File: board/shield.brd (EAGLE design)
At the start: 66 x 57.8 mm, 44 parts, among them IC1 LM75, J1 WEALTHMETAL DS-214B, J2 22-05-7028-02, J3 22-05-7038-03, K1 G5L, T1 BC817, U1 LM2596S-5.0

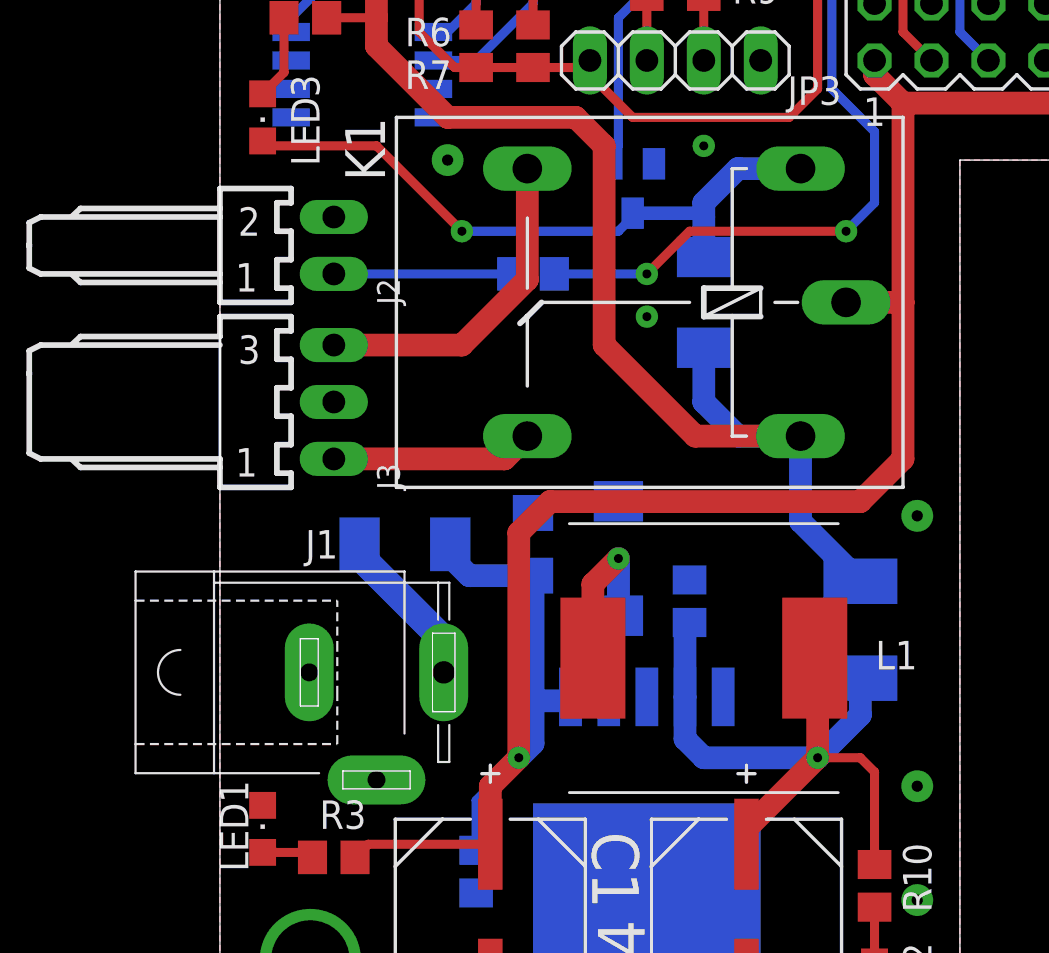
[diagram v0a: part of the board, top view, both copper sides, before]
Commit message: DC Jack connector replaced
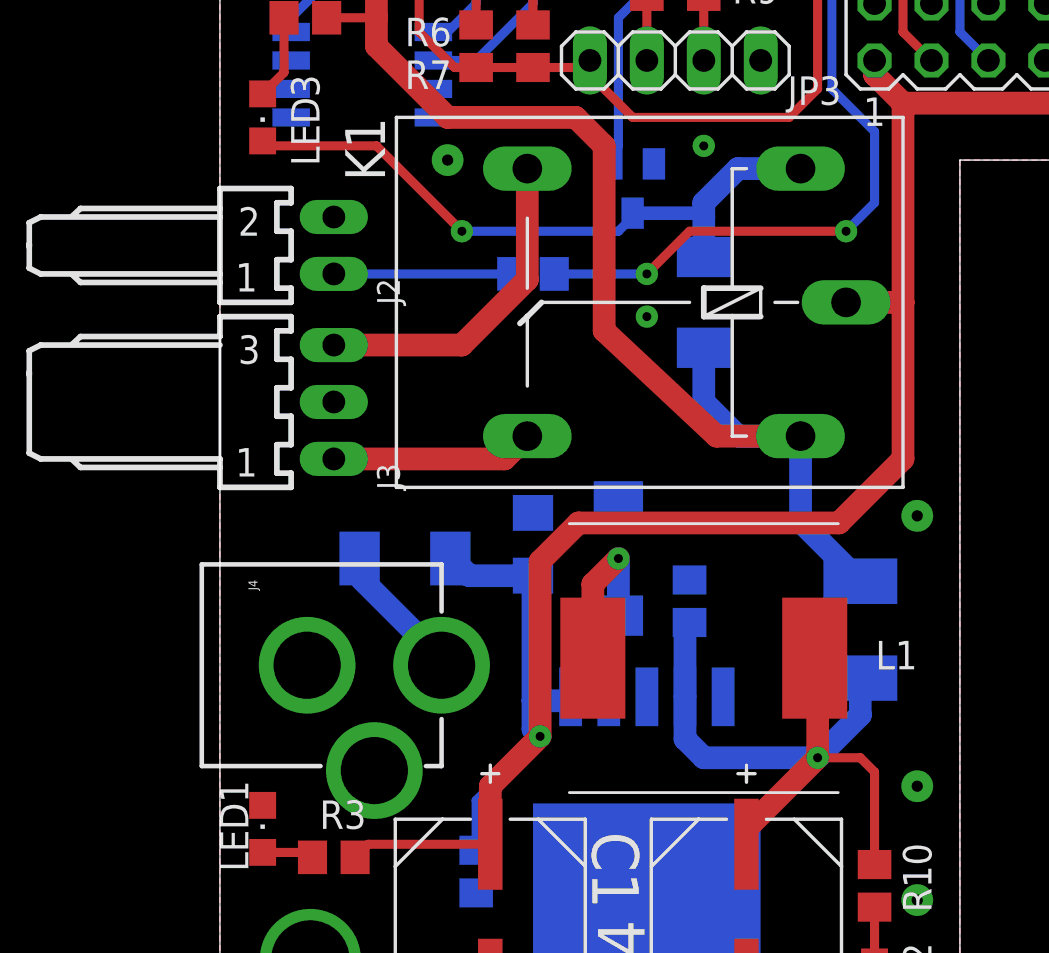
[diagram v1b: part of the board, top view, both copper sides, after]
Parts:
- removed J1: WEALTHMETAL DS-214B, con-jack:SPC4077
- added J4: POWER_JACKPTH, SparkFun-Connectors:POWER_JACK_PTH
- moved D3 0.63 mm to (8.26, 22.2)
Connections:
- net GND: now also J4.GND, J4.GNDBREAK; no longer J1.1, J1.2
- net UIN: now also J4.PWR; no longer J1.3
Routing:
- net +24V: track 98.0 -> 96.4 mm

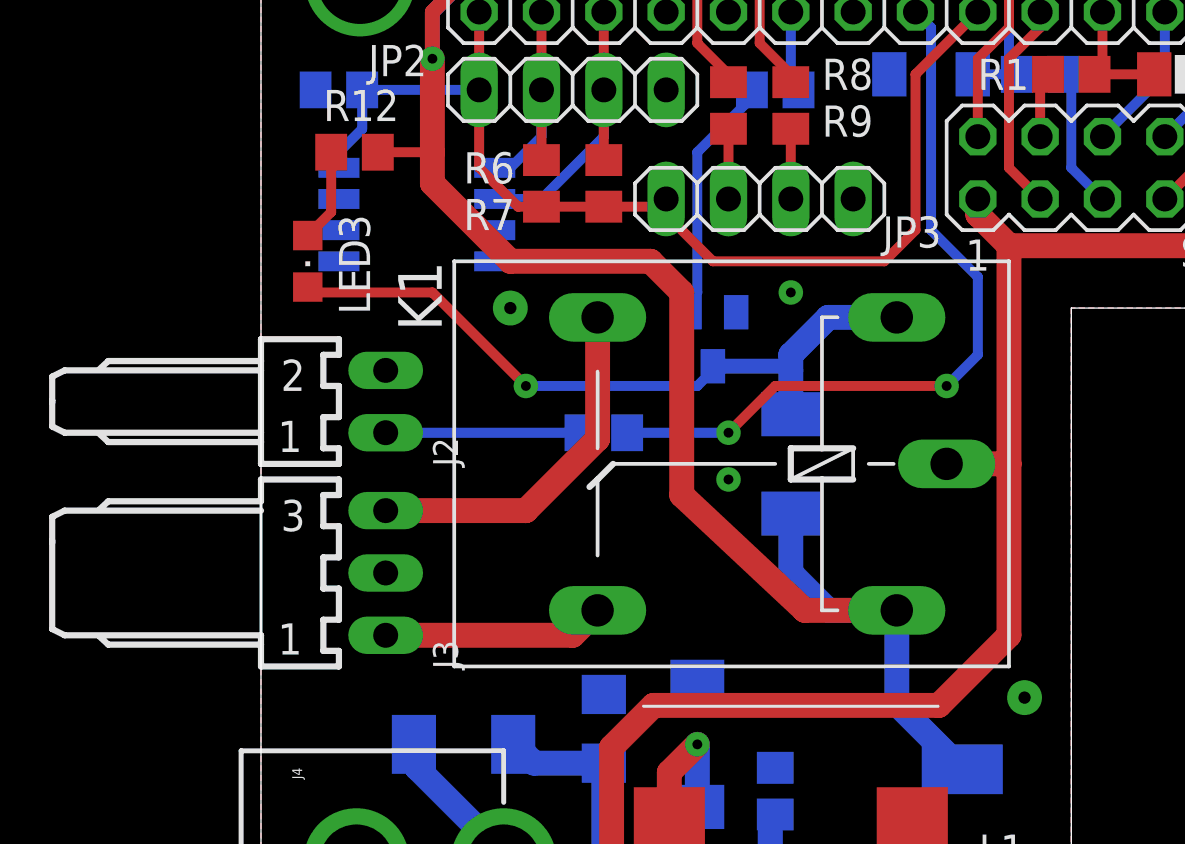
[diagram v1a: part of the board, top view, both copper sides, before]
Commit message: Relay connector extended with common pin, connection to +24V is optional by solder bridge
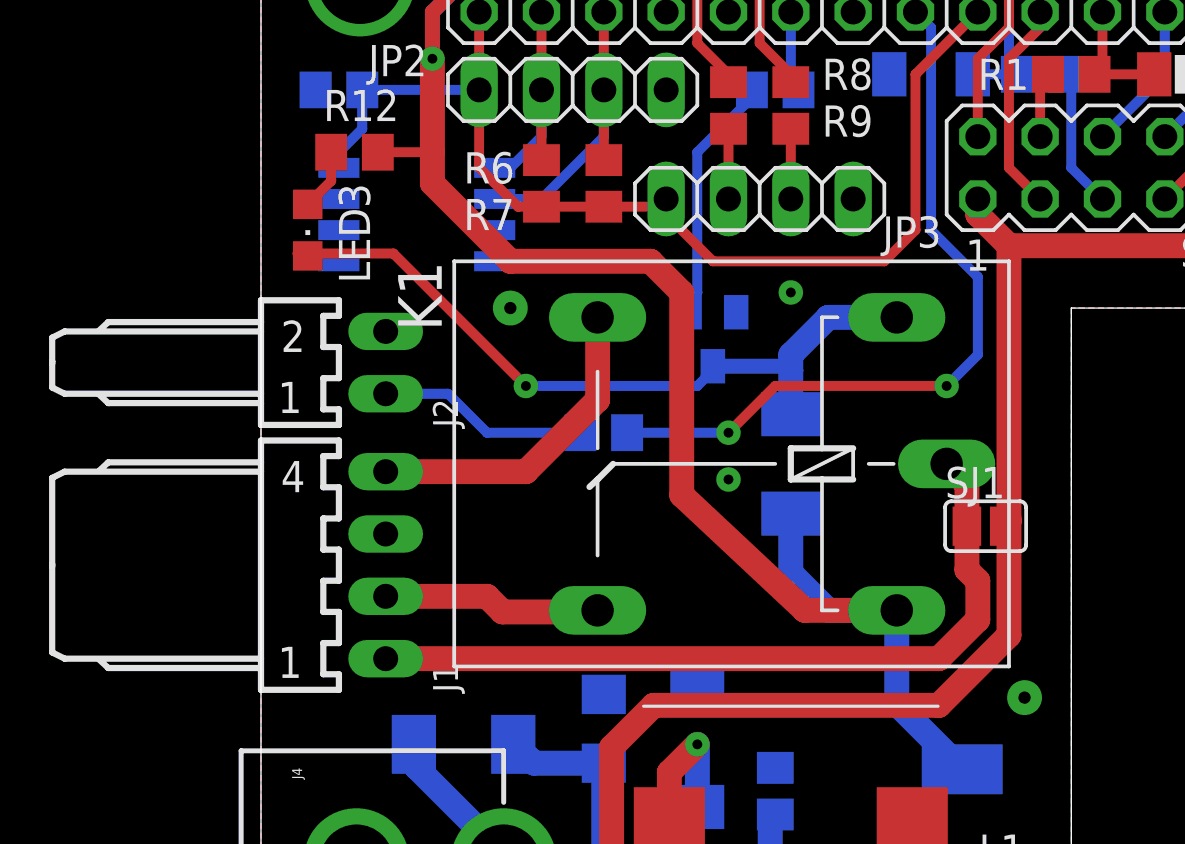
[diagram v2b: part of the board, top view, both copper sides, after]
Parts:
- removed J3: 22-05-7038-03, con-molex:7395-03
- added J1: 22-05-7048-04, con-molex:7395-04
- added SJ1: (no value), jumper:SJ
- moved J2 1.59 mm to (5.08, 37.8)
- moved LED3 1.27 mm to (1.91, 43.2)
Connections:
- net N$10 renamed LOCK_T1_R
- net N$11 renamed LED
- net N$8 renamed RELAY_SW
- removed net N$5: J3.3, K1.S
- removed net N$7: J3.1, K1.O
- new net C: J1.1, K1.P, SJ1.1
- new net NC: J1.2, K1.O
- new net NO: J1.4, K1.S
- net +24V: now also SJ1.2; no longer K1.P
- net GND: now also J1.3; no longer J3.2
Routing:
- net C: track 0.00 -> 31.7 mm
- net N$5: track 14.8 -> 0.00 mm
- net NO: track 0.00 -> 13.2 mm
- net N$7: track 9.06 -> 0.00 mm
- net NC: track 0.00 -> 8.93 mm
- net +24V: track 96.4 -> 94.2 mm
- net RELAY_SW: track 29.2 -> 30.6 mm
- net LED: track 3.79 -> 2.52 mm
- net N$2: track 7.94 -> 8.60 mm
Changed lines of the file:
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@@
 </element>
 <element name="PCB1" library="e14_Rpi3_RevA" package="RPI3" value="RPI3" x="122.36" y="-1.375" rot="R90"/>
-<element name="J2" library="con-molex" package="7395-02" value="22-05-7028-02" x="5.08" y="36.195" rot="R270">
-<attribute name="OC_FARNELL" value="9731601" x="5.08" y="36.195" size="1.778" layer="27" rot="R270" display="off"/>
-<attribute name="MPN" value="" x="5.08" y="36.195" size="1.778" layer="27" rot="R270" display="off"/>
-<attribute name="OC_NEWARK" value="unknown" x="5.08" y="36.195" size="1.778" layer="27" rot="R270" display="off"/>
-<attribute name="MF" value="" x="5.08" y="36.195" size="1.778" layer="27" rot="R270" display="off"/>
-</element>
-<element name="J3" library="con-molex" package="7395-03" value="22-05-7038-03" x="5.08" y="29.21" rot="R270">
-<attribute name="OC_FARNELL" value="unknown" x="5.08" y="29.21" size="1.778" layer="27" rot="R270" display="off"/>
-<attribute name="MPN" value="" x="5.08" y="29.21" size="1.778" layer="27" rot="R270" display="off"/>
-<attribute name="OC_NEWARK" value="unknown" x="5.08" y="29.21" size="1.778" layer="27" rot="R270" display="off"/>
-<attribute name="MF" value="" x="5.08" y="29.21" size="1.778" layer="27" rot="R270" display="off"/>
+<element name="J2" library="con-molex" package="7395-02" value="22-05-7028-02" x="5.08" y="37.7825" rot="R270">
+<attribute name="OC_FARNELL" value="9731601" x="5.08" y="37.7825" size="1.778" layer="27" rot="R270" display="off"/>
+<attribute name="MPN" value="" x="5.08" y="37.7825" size="1.778" layer="27" rot="R270" display="off"/>
+<attribute name="OC_NEWARK" value="unknown" x="5.08" y="37.7825" size="1.778" layer="27" rot="R270" display="off"/>
+<attribute name="MF" value="" x="5.08" y="37.7825" size="1.778" layer="27" rot="R270" display="off"/>
 </element>
 <element name="SV1" library="con-lstb" package="MA05-2" value="S2G10" x="34.29" y="45.72" smashed="yes">
@@
 <attribute name="VALUE" x="4.445" y="48.895" size="1.27" layer="27" rot="R180"/>
 </element>
-<element name="LED3" library="led" package="CHIPLED_0805" value="SML-LX0805SUGC-TR" x="1.905" y="41.91" smashed="yes" rot="R180">
-<attribute name="NAME" x="3.175" y="43.815" size="1.27" layer="25" rot="R270"/>
-<attribute name="VALUE" x="-0.635" y="43.18" size="1.27" layer="27" rot="R270"/>
+<element name="LED3" library="led" package="CHIPLED_0805" value="SML-LX0805SUGC-TR" x="1.905" y="43.18" smashed="yes" rot="R180">
+<attribute name="NAME" x="3.175" y="45.085" size="1.27" layer="25" rot="R270"/>
+<attribute name="VALUE" x="-0.635" y="44.45" size="1.27" layer="27" rot="R270"/>
 </element>
 <element name="C6" library="rcl" package="C0805" value="100n" x="3.175" y="48.895" rot="MR180"/>
@@
 <attribute name="PROD_ID" value="CONN-08197" x="-3.81" y="17.4625" size="1.778" layer="27" rot="R270" display="off"/>
 </element>
+<element name="J1" library="con-molex" package="7395-04" value="22-05-7048-04" x="5.08" y="29.5275" rot="R270">
+<attribute name="MF" value="" x="5.08" y="29.5275" size="1.778" layer="27" rot="R270" display="off"/>
+<attribute name="MPN" value="" x="5.08" y="29.5275" size="1.778" layer="27" rot="R270" display="off"/>
+<attribute name="OC_FARNELL" value="unknown" x="5.08" y="29.5275" size="1.778" layer="27" rot="R270" display="off"/>
+<attribute name="OC_NEWARK" value="unknown" x="5.08" y="29.5275" size="1.778" layer="27" rot="R270" display="off"/>
+</element>
+<element name="SJ1" library="jumper" package="SJ" value="" x="29.5275" y="31.115"/>
 </elements>
 <signals>
@@
 <contactref element="T1" pad="E"/>
 <contactref element="J2" pad="2"/>
-<contactref element="J3" pad="2"/>
 <polygon width="0.4064" layer="1" isolate="0.3048">
 <vertex x="0" y="57.785"/>
@@
 <contactref element="J4" pad="GNDBREAK"/>
 <contactref element="J4" pad="GND"/>
+<contactref element="J1" pad="3"/>
 </signal>
 <signal name="+24V">
@@
 <contactref element="C1" pad="1"/>
 <contactref element="R3" pad="2"/>
-<contactref element="K1" pad="P"/>
 <wire x1="14.2875" y1="14.2875" x2="13.97" y2="14.605" width="1.016" layer="16"/>
 <wire x1="13.97" y1="14.605" x2="13.97" y2="15.875" width="1.016" layer="16"/>
@@
 <wire x1="46.99" y1="43.815" x2="45.72" y2="42.545" width="1.016" layer="1"/>
 <wire x1="45.72" y1="42.545" x2="30.48" y2="42.545" width="1.016" layer="1"/>
-<wire x1="30.48" y1="42.545" x2="30.48" y2="33.655" width="1.016" layer="1"/>
-<wire x1="30.48" y1="33.655" x2="30.48" y2="26.67" width="1.016" layer="1"/>
+<wire x1="30.48" y1="42.545" x2="30.48" y2="31.4325" width="1.016" layer="1"/>
+<wire x1="30.48" y1="31.3055" x2="30.48" y2="26.67" width="1.016" layer="1"/>
 <wire x1="30.48" y1="26.67" x2="27.6225" y2="23.8125" width="1.016" layer="1"/>
-<wire x1="27.94" y1="33.655" x2="30.48" y2="33.655" width="1.016" layer="1"/>
 <wire x1="15.995" y1="23.8125" x2="27.6225" y2="23.8125" width="1.016" layer="1"/>
 <wire x1="12.065" y1="9.4742" x2="12.065" y2="12.065" width="1.016" layer="1"/>
@@
 <wire x1="14.2875" y1="22.105" x2="14.2875" y2="14.2875" width="1.016" layer="1"/>
 <wire x1="10.36" y1="22.225" x2="10.28" y2="22.225" width="0.4064" layer="16"/>
+<contactref element="SJ1" pad="2"/>
+<wire x1="30.2895" y1="31.115" x2="30.48" y2="31.3055" width="1.016" layer="1"/>
+<wire x1="30.48" y1="31.3055" x2="30.48" y2="31.4325" width="1.016" layer="1"/>
 </signal>
 <signal name="N$4">
@@
 <contactref element="R11" pad="1"/>
 <contactref element="J2" pad="1"/>
-<wire x1="5.08" y1="34.925" x2="13.02" y2="34.925" width="0.4064" layer="16"/>
-</signal>
-<signal name="N$5">
-<contactref element="J3" pad="3"/>
+<wire x1="5.08" y1="36.5125" x2="7.62" y2="36.5125" width="0.4064" layer="16"/>
+<wire x1="7.62" y1="36.5125" x2="9.2075" y2="34.925" width="0.4064" layer="16"/>
+<wire x1="9.2075" y1="34.925" x2="13.02" y2="34.925" width="0.4064" layer="16"/>
+</signal>
+<signal name="NO">
 <contactref element="K1" pad="S"/>
-<wire x1="5.08" y1="31.75" x2="10.795" y2="31.75" width="1.016" layer="1"/>
-<wire x1="10.795" y1="31.75" x2="13.716" y2="34.671" width="1.016" layer="1"/>
-<wire x1="13.716" y1="34.671" x2="13.716" y2="39.624" width="1.016" layer="1"/>
-</signal>
-<signal name="N$8">
+<wire x1="5.08" y1="33.3375" x2="10.795" y2="33.3375" width="1.016" layer="1"/>
+<wire x1="10.795" y1="33.3375" x2="13.716" y2="36.2585" width="1.016" layer="1"/>
+<wire x1="13.716" y1="36.2585" x2="13.716" y2="39.624" width="1.016" layer="1"/>
+<contactref element="J1" pad="4"/>
+</signal>
+<signal name="RELAY_SW">
 <contactref element="T1" pad="C"/>
 <contactref element="D7" pad="A"/>
@@
 <wire x1="18.245" y1="37.295" x2="18.245" y2="37.465" width="0.4064" layer="16"/>
 <wire x1="18.245" y1="37.465" x2="18.415" y2="37.635" width="0.4064" layer="16"/>
-<wire x1="10.795" y1="36.83" x2="6.985" y2="40.64" width="0.4064" layer="1"/>
-<wire x1="1.905" y1="40.86" x2="2.125" y2="40.64" width="0.4064" layer="1"/>
-<wire x1="2.125" y1="40.64" x2="6.985" y2="40.64" width="0.4064" layer="1"/>
-</signal>
-<signal name="N$10">
+<wire x1="10.795" y1="36.83" x2="5.3975" y2="42.2275" width="0.4064" layer="1"/>
+<wire x1="1.905" y1="42.13" x2="1.49" y2="42.2275" width="0.4064" layer="1"/>
+<wire x1="1.49" y1="42.2275" x2="5.3975" y2="42.2275" width="0.4064" layer="1"/>
+</signal>
+<signal name="LOCK_T1_R">
 <contactref element="T1" pad="B"/>
 <contactref element="R13" pad="1"/>
@@
 <wire x1="28.575" y1="13.335" x2="26.67" y2="13.335" width="0.4064" layer="1"/>
 </signal>
-<signal name="N$7">
-<contactref element="J3" pad="1"/>
+<signal name="NC">
 <contactref element="K1" pad="O"/>
-<wire x1="13.716" y1="27.686" x2="12.7" y2="26.67" width="1.016" layer="1"/>
-<wire x1="12.7" y1="26.67" x2="5.08" y2="26.67" width="1.016" layer="1"/>
+<wire x1="5.08" y1="28.2575" x2="9.2075" y2="28.2575" width="1.016" layer="1"/>
+<wire x1="9.2075" y1="28.2575" x2="9.8425" y2="27.6225" width="1.016" layer="1"/>
+<wire x1="9.8425" y1="27.6225" x2="13.6525" y2="27.6225" width="1.016" layer="1"/>
+<wire x1="13.6525" y1="27.6225" x2="13.716" y2="27.686" width="1.016" layer="1"/>
+<contactref element="J1" pad="2"/>
 </signal>
 <signal name="I-D0-3V3">
@@
 <wire x1="6.35" y1="22.105" x2="6.23" y2="22.225" width="1.016" layer="16"/>
 </signal>
-<signal name="N$11">
+<signal name="LED">
 <contactref element="R12" pad="2"/>
 <contactref element="LED3" pad="A"/>
-<wire x1="1.905" y1="42.96" x2="2.86" y2="43.915" width="0.4064" layer="1"/>
-<wire x1="2.86" y1="43.915" x2="2.86" y2="46.355" width="0.4064" layer="1"/>
+<wire x1="1.905" y1="44.23" x2="2.86" y2="45.185" width="0.4064" layer="1"/>
+<wire x1="2.86" y1="45.185" x2="2.86" y2="46.355" width="0.4064" layer="1"/>
+</signal>
+<signal name="C">
+<contactref element="K1" pad="P"/>
+<contactref element="J1" pad="1"/>
+<contactref element="SJ1" pad="1"/>
+<wire x1="5.08" y1="25.7175" x2="27.6225" y2="25.7175" width="1.016" layer="1"/>
+<wire x1="27.6225" y1="25.7175" x2="29.21" y2="27.305" width="1.016" layer="1"/>
+<wire x1="29.21" y1="27.305" x2="29.21" y2="28.8925" width="1.016" layer="1"/>
+<wire x1="29.21" y1="28.8925" x2="28.7655" y2="29.337" width="1.016" layer="1"/>
+<wire x1="28.7655" y1="29.337" x2="28.7655" y2="31.115" width="1.016" layer="1"/>
+<wire x1="27.94" y1="33.655" x2="28.7655" y2="32.8295" width="1.016" layer="1"/>
+<wire x1="28.7655" y1="32.8295" x2="28.7655" y2="31.115" width="1.016" layer="1"/>
 </signal>
 </signals>
